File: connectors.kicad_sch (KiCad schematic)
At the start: 0 parts

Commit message: added components
servo controller, esp32
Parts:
- added J15: Conn_01x08, Connector_PinHeader_2.54mm:PinHeader_1x08_P2.54mm_Vertical, symbol Connector_Generic:Conn_01x08
- added J16, J17: Conn_01x08, symbol Connector_Generic:Conn_01x08
- added R31, R32, R33, R34, R35, R36, R37, R38: 12k, Resistor_SMD:R_0805_2012Metric, symbol Device:R_Small
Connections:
- new net: J15.1 (Pin_1), R31.1
- new net: J15.8 (Pin_8), R38.1
- new net: J15.2 (Pin_2), R32.1
- new net: J15.3 (Pin_3), R33.1
- new net: J15.4 (Pin_4), R34.1
- new net: J15.5 (Pin_5), R35.1
- new net: J15.6 (Pin_6), R36.1
- new net: J15.7 (Pin_7), R37.1
- new net 5V2: J16.1 (Pin_1), J16.2 (Pin_2), J16.3 (Pin_3), J16.4 (Pin_4), J16.5 (Pin_5), J16.6 (Pin_6), J16.7 (Pin_7), J16.8 (Pin_8)
- new net GND: J17.1 (Pin_1), J17.2 (Pin_2), J17.3 (Pin_3), J17.4 (Pin_4), J17.5 (Pin_5), J17.6 (Pin_6), J17.7 (Pin_7), J17.8 (Pin_8)
- new net PCA_0: R31.2
- new net PCA_1: R32.2
- new net PCA_2: R33.2
- new net PCA_3: R34.2
- new net PCA_4: R35.2
- new net PCA_5: R36.2
- new net PCA_6: R37.2
- new net PCA_7: R38.2

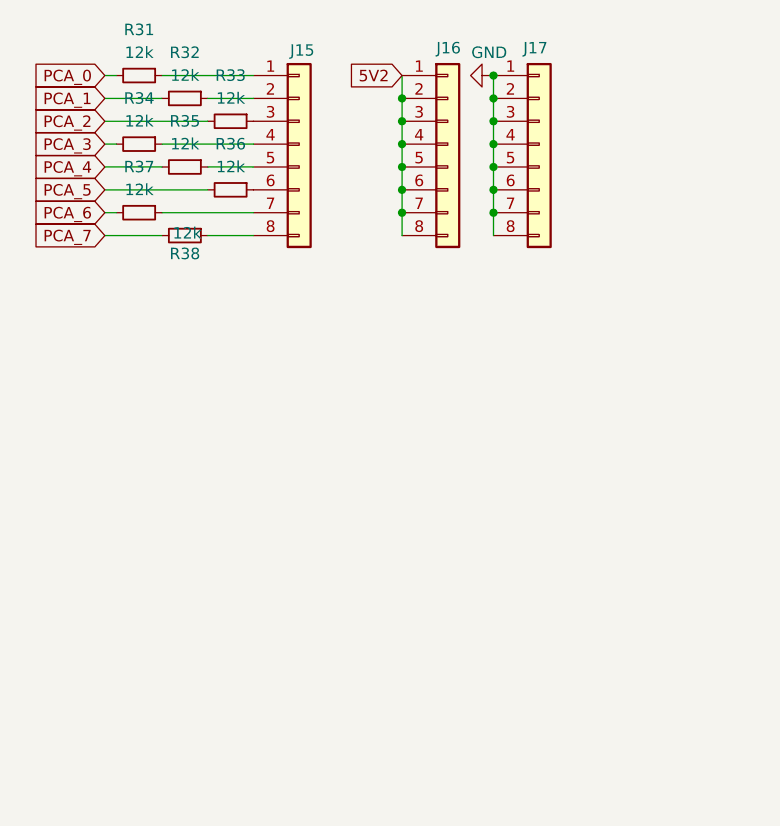
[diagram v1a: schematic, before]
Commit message: some connectors added
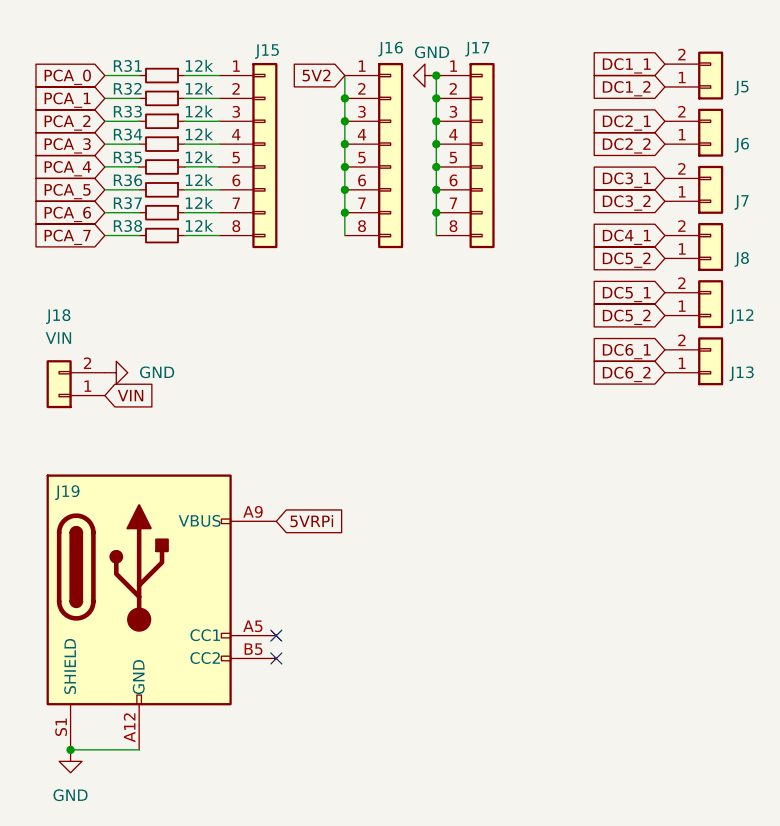
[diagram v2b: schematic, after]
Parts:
- added J12, J13, J5, J6, J7, J8: Conn_01x02, Connector_JST:JST_XH_S2B-XH-A-1_1x02_P2.50mm_Horizontal, symbol Connector_Generic:Conn_01x02
- added J18: VIN, Connector_AMASS:AMASS_XT60PW-F_1x02_P7.20mm_Horizontal, symbol Connector_Generic:Conn_01x02
- added J19: USB_C_Receptacle_PowerOnly_6P, Connector_USB:USB_C_Receptacle_GCT_USB4125-xx-x_6P_TopMnt_Horizontal, symbol Connector:USB_C_Receptacle_PowerOnly_6P
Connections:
- net GND: now also J18.2 (Pin_2), J19.A12 (GND), J19.B12 (GND), J19.S1 (SHIELD)
- new net 5VRPi: J19.A9 (VBUS), J19.B9 (VBUS)
- new net DC1_1: J5.2 (Pin_2)
- new net DC1_2: J5.1 (Pin_1)
- new net DC2_1: J6.2 (Pin_2)
- new net DC2_2: J6.1 (Pin_1)
- new net DC3_1: J7.2 (Pin_2)
- new net DC3_2: J7.1 (Pin_1)
- new net DC4_1: J8.2 (Pin_2)
- new net DC5_1: J12.2 (Pin_2)
- new net DC5_2: J12.1 (Pin_1), J8.1 (Pin_1)
- new net DC6_1: J13.2 (Pin_2)
- new net DC6_2: J13.1 (Pin_1)
- new net VIN: J18.1 (Pin_1)
- no-connect marks 0 -> 2
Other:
- moved on the sheet: J15, J16, J17, R31

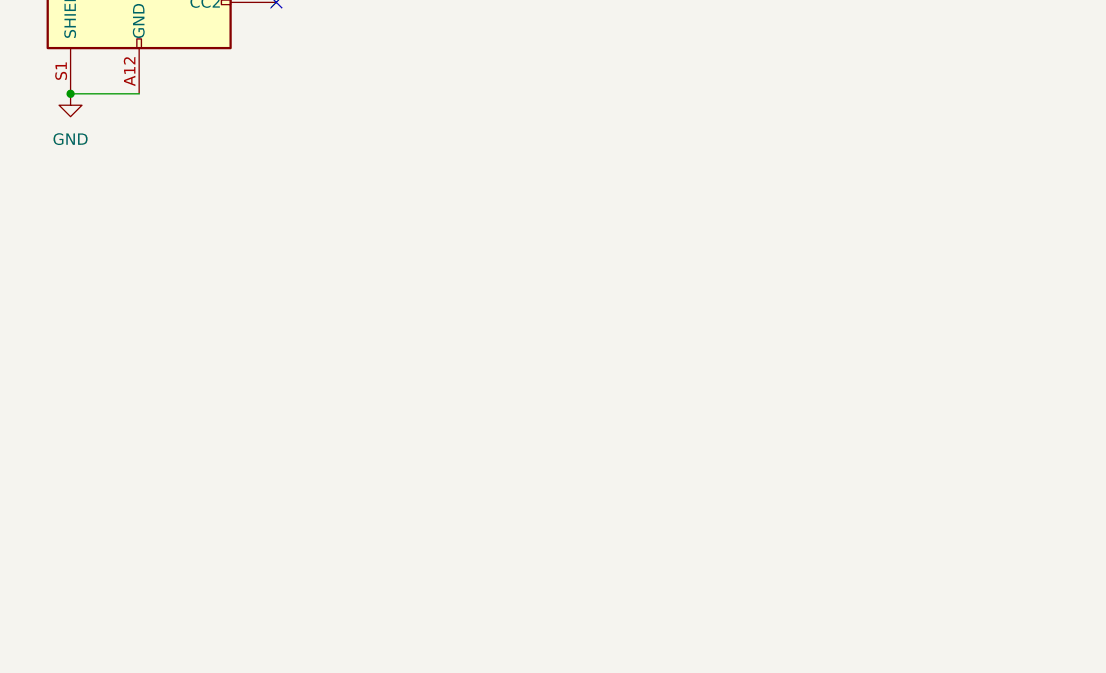
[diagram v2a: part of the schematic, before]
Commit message: gpio expander added comm finished
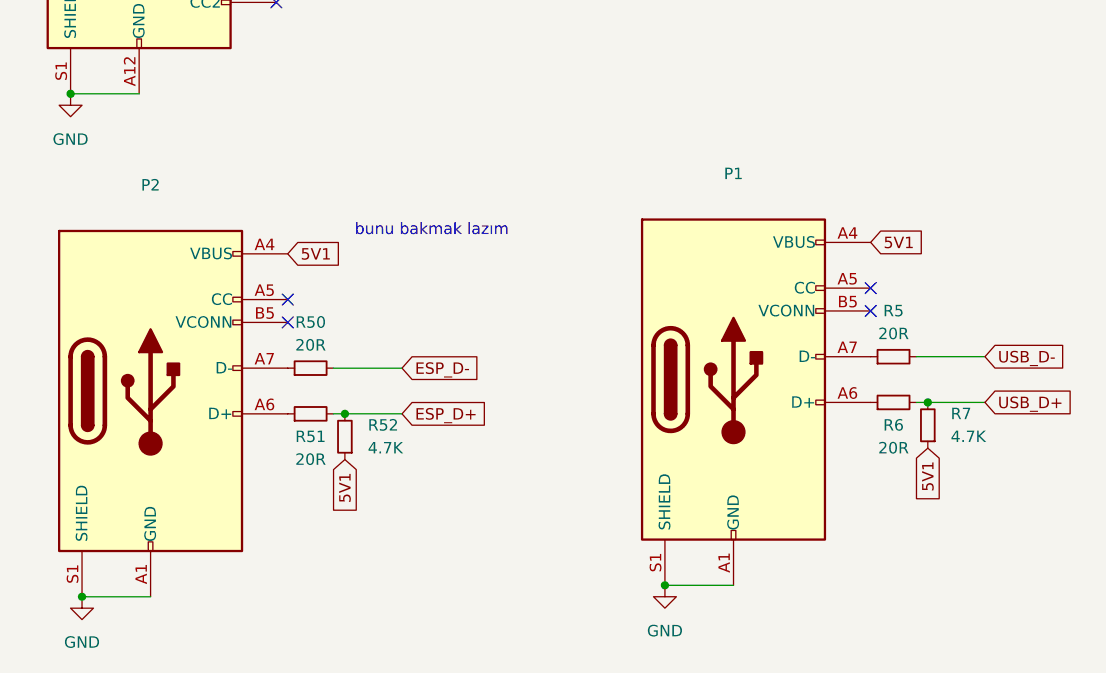
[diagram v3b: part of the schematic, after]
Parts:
- added P1, P2: USB_C_Plug_USB2.0, symbol Connector:USB_C_Plug_USB2.0
- added R5, R50, R51, R6: 20R, Resistor_SMD:R_0805_2012Metric, symbol Device:R_Small
- added R52, R7: 4.7K, Resistor_SMD:R_0805_2012Metric, symbol Device:R_Small
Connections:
- net GND: now also P1.A1 (GND), P1.A12 (GND), P1.B1 (GND), P1.B12 (GND), P1.S1 (SHIELD), P2.A1 (GND), P2.A12 (GND), P2.B1 (GND), P2.B12 (GND), P2.S1 (SHIELD)
- new net: P1.A6 (D+), R6.1
- new net: P1.A7 (D-), R5.1
- new net: P2.A6 (D+), R51.1
- new net: P2.A7 (D-), R50.1
- new net 5V1: P1.A4 (VBUS), P1.A9 (VBUS), P1.B4 (VBUS), P1.B9 (VBUS), P2.A4 (VBUS), P2.A9 (VBUS), P2.B4 (VBUS), P2.B9 (VBUS), R52.1, R7.1
- new net ESP_D+: R51.2, R52.2
- new net ESP_D-: R50.2
- new net USB_D+: R6.2, R7.2
- new net USB_D-: R5.2
- no-connect marks 2 -> 6
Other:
- note added: "bunu bakmak lazım"

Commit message: Visual Improvements
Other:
- note added: "DC Motor Outs"
- note added: "ESP32 USB"
- note added: "Power In Connector"
- note added: "RPi Power Out"
- note added: "STM32 USB"
- note added: "Servo Motor Outs"
- moved on the sheet: J12, J13, J15, J16, J17, J18, J19, J5, J6, J7, J8, P1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

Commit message: schematic finished
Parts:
- removed P1, P2: USB_C_Plug_USB2.0, symbol Connector:USB_C_Plug_USB2.0
- removed R50, R51: 20R, Resistor_SMD:R_0805_2012Metric, symbol Device:R_Small
- removed R52: 4.7K, Resistor_SMD:R_0805_2012Metric, symbol Device:R_Small
- added D26, D31: 1N5819, Diode_SMD:D_SOD-123, symbol Device:D_Zener_Small_Filled
- added D27, D28, D29, D30: ESD05V88D-LC, Diode_SMD:D_SOD-882, symbol Device:D_TVS
- added J14, J15: USB_C_Receptacle_USB2.0_16P, Connector_USB:USB_C_Receptacle_Palconn_UTC16-G, symbol Connector:USB_C_Receptacle_USB2.0_16P
- added R45, R47: 20R, Resistor_SMD:R_0805_2012Metric, symbol Device:R_Small
- added R49: 4.7K, Resistor_SMD:R_0805_2012Metric, symbol Device:R_Small
- J5: renamed from J16; footprint (none) -> Connector_PinHeader_2.54mm:PinHeader_1x08_P2.54mm_Vertical
- J6: renamed from J17; footprint (none) -> Connector_PinHeader_2.54mm:PinHeader_1x08_P2.54mm_Vertical
- renumbered J7 to J10, J6 to J11, J5 to J12, J19 to J13, J18 to J3, J15 to J4, J13 to J7, J12 to J8, J8 to J9, R31 to R37, R32 to R38, R33 to R39, R34 to R40, R35 to R41, R36 to R42, R37 to R43, R38 to R44, R5 to R46, R6 to R48, R7 to R50
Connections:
- net 5V1: now also D26.1 (K), D31.1 (K), R49.1
- net ESP_D+: now also D27.2 (A2), R47.2, R49.2
- net ESP_D-: now also D28.2 (A2), R45.2
- net GND: now also D27.1 (A1), D28.1 (A1), D29.1 (A1), D30.1 (A1), J14.A1 (GND), J14.A12 (GND), J14.B1 (GND), J14.B12 (GND), J14.S1 (SHIELD), J15.A1 (GND), J15.A12 (GND), J15.B1 (GND), J15.B12 (GND), J15.S1 (SHIELD)
- net USB_D+: now also D29.2 (A2)
- net USB_D-: now also D30.2 (A2)
- net at R48.1: now also J15.A6 (D+), J15.B6 (D+)
- net at R46.1: now also J15.A7 (D-), J15.B7 (D-)
- new net: D26.2 (A), J14.A4 (VBUS), J14.A9 (VBUS), J14.B4 (VBUS), J14.B9 (VBUS)
- new net: J14.A7 (D-), J14.B7 (D-), R45.1
- new net: D31.2 (A), J15.A4 (VBUS), J15.A9 (VBUS), J15.B4 (VBUS), J15.B9 (VBUS)
- new net: J14.A6 (D+), J14.B6 (D+), R47.1
- no-connect marks 6 -> 10
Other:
- note removed: "STM32 USB"
- note removed: "bunu bakmak lazım"
- moved on the sheet: R46, R48, R50

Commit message: Reapply "placing completed."
This reverts commit 83f85ef5575867dc78eeeae3514badb4960c2205.
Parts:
- added C7: 220uF 35V, Capacitor_SMD:CP_Elec_8x10.5, symbol Device:C_Polarized_Small
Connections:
- net 5V2: now also C7.1
- net DC5_2: no longer J9.1 (Pin_1)
- net GND: now also C7.2
- new net DC4_2: J9.1 (Pin_1)
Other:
- moved on the sheet: J5, J6

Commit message: esp32 silindi, yerleştirmeler yapıldı
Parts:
- removed D26, D31: 1N5819, Diode_SMD:D_SOD-123, symbol Device:D_Zener_Small_Filled
- removed D27, D28, D29, D30: ESD05V88D-LC, Diode_SMD:D_SOD-882, symbol Device:D_TVS
- removed J14, J15: USB_C_Receptacle_USB2.0_16P, Connector_USB:USB_C_Receptacle_Palconn_UTC16-G, symbol Connector:USB_C_Receptacle_USB2.0_16P
- removed R45, R46, R47, R48: 20R, Resistor_SMD:R_0805_2012Metric, symbol Device:R_Small
- removed R49, R50: 4.7K, Resistor_SMD:R_0805_2012Metric, symbol Device:R_Small
- added J14: STM_UART, Connector_PinHeader_2.54mm:PinHeader_1x04_P2.54mm_Vertical, symbol Connector_Generic:Conn_01x04
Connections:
- net DC1_1: now also J12.1 (Pin_1); no longer J12.2 (Pin_2)
- net DC1_2: now also J12.2 (Pin_2); no longer J12.1 (Pin_1)
- net DC2_1: now also J11.1 (Pin_1); no longer J11.2 (Pin_2)
- net DC2_2: now also J11.2 (Pin_2); no longer J11.1 (Pin_1)
- net DC3_1: now also J10.1 (Pin_1); no longer J10.2 (Pin_2)
- net DC3_2: now also J10.2 (Pin_2); no longer J10.1 (Pin_1)
- net DC4_1: now also J9.1 (Pin_1); no longer J9.2 (Pin_2)
- net DC4_2: now also J9.2 (Pin_2); no longer J9.1 (Pin_1)
- net DC5_1: now also J8.1 (Pin_1); no longer J8.2 (Pin_2)
- net DC5_2: now also J8.2 (Pin_2); no longer J8.1 (Pin_1)
- net DC6_1: now also J7.1 (Pin_1); no longer J7.2 (Pin_2)
- net DC6_2: now also J7.2 (Pin_2); no longer J7.1 (Pin_1)
- net GND: now also J14.4 (Pin_4)
- new net 3V3: J14.1 (Pin_1)
- new net USART1_RX: J14.2 (Pin_2)
- new net USART1_TX: J14.3 (Pin_3)
- no-connect marks 10 -> 2
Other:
- note removed: "ESP32 USB"
